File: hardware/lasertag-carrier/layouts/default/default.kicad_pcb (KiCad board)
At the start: 2 copper layers, 100 x 80 mm, 39 parts, among them J0 Power in 2P, J1 S3-Matrix L, J12 Ext button, J13 Touch hdr, J14 Activity LED, J2 S3-Matrix R, J3 MAX98357A, J4 Speaker, J5 microSD, J6 IR RX, J7 IR LED, J8 WS2812 out, J9 OLED I2C, Q1 2N2222A, SW1 SW_PUSH_6mm, SW2 PWR switch

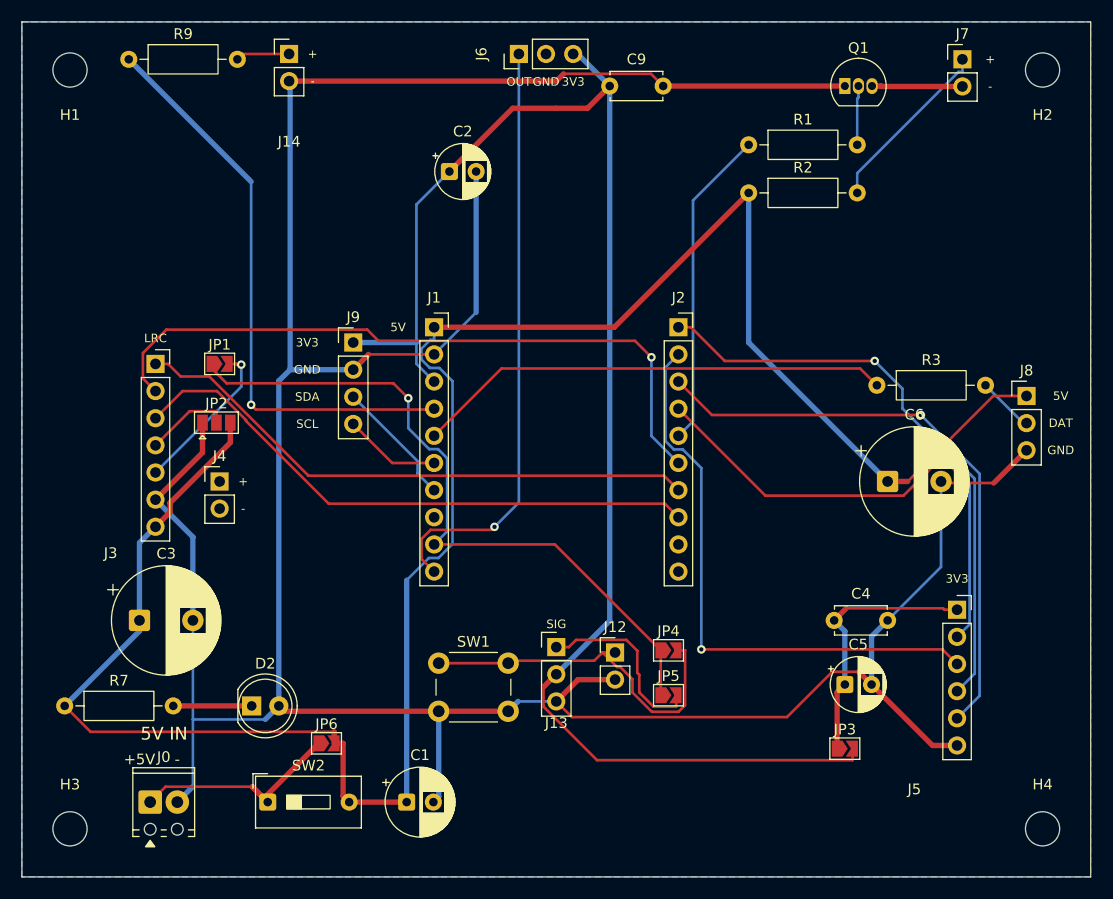
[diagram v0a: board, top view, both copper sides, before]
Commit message: Silk: component values and socket/function names
- resistor values inside each body: 470R/33R (IR), 220R (WS + ACT), 330R (PWR)
- capacitor values alongside: 100u, 10u x2, 470u, 1000u, 100n x2
- 2N2222A by Q1, PWR by D2
- jumper functions: MUTE, GAIN, VDD, BTN, TOUCH, ON
- socket names: AUDIO and microSD rotated under their breakout bodies
  (visible when empty, covered by the module itself once populated),
  plus OLED, WS2812, TOUCH, BTN, SPKR, IR-TX, IR-RX, ACT, PWR
- refdes relocations to clear the new text (J7/J9/JP1/JP6/J12/Q1)

DRC: 0 unconnected, 0 electrical. Three phantom silk_overlap warnings
remain - kicad-cli 10.0.3 pairs reference fields with items 10-60mm away
(J6 ref vs its own segment AND vs WS2812 text 50mm off; C9 ref vs 100n
60mm off). Geometrically impossible; silk Gerber verified.

Fab zip regenerated.

Co-Authored-By: Claude Opus 4.8 <noreply@anthropic.com>
Claude-Session: https://claude.ai/code/session_01TutNLcDSScdeeVSbjpyg8j
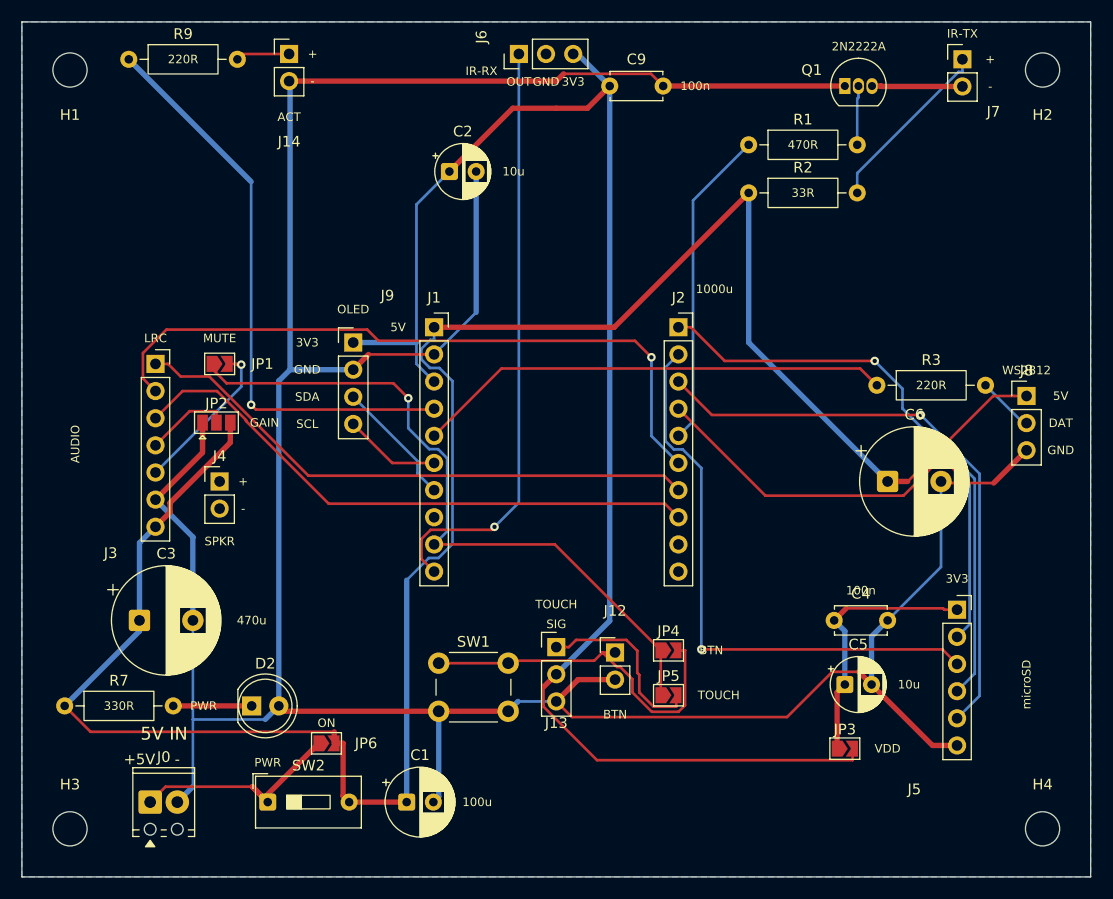
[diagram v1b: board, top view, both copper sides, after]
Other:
- board text added: "1000u"
- board text added: "100n"
- board text added: "100u"
- board text added: "10u"
- board text added: "220R"
- board text added: "2N2222A"
- board text added: "330R"
- board text added: "33R"
- board text added: "470R"
- board text added: "470u"
- board text added: "ACT"
- board text added: "AUDIO"
- board text added: "BTN"
- board text added: "GAIN"
- board text added: "IR-RX"
- board text added: "IR-TX"
- board text added: "MUTE"
- board text added: "OLED"
- board text added: "ON"
- board text added: "PWR"
- board text added: "SPKR"
- board text added: "TOUCH"
- board text added: "VDD"
- board text added: "WS2812"
- board text added: "microSD"

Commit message: Label polish per review; remove superfluous speaker header J4
- 1000u moved inside C6's can (was floating 8mm right of it)
- AUDIO snugged against the J3 socket
- ACT -> ACT LED
- 100n moved inside C9's box (fits between the pads)
- 10u placed vertically beside C5 -- the D5 can physically cannot fit
  0.8mm text between its silk circle and the pad copper (24 arc-segment
  DRC hits proved it)
- J4 removed: its nets appeared nowhere else on the board -- the
  MAX98357A module carries its own speaker terminals (Assumption #10),
  so the header was an unconnected landing pad with no route. BOM and
  i2s_audio.ato updated.

DRC: 0 unconnected, 0 electrical, 3 known-phantom silk warnings.
Fab zip regenerated.

Co-Authored-By: Claude Opus 4.8 <noreply@anthropic.com>
Claude-Session: https://claude.ai/code/session_01TutNLcDSScdeeVSbjpyg8j
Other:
- board text added: "ACT LED"
- board text removed: "ACT"
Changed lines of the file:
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@@
 		)
 	)
-	(gr_text "ACT"
+	(gr_text "ACT LED"
 		(at 125 68.9 0)
 		(layer "F.SilkS")
@@
 		)
 	)
+	(gr_text "1000u"
+		(at 157 82.5 0)
+		(layer "F.SilkS")
+		(effects
+			(font
+				(size 0.8 0.8)
+				(thickness 0.13)
+			)
+		)
+	)
 	(gr_text "100n"
-		(at 163 66 0)
+		(at 157.5 66 0)
 		(layer "F.SilkS")
 		(effects
@@
 		)
 	)
-	(gr_text "1000u"
-		(at 164.8 85 0)
-		(layer "F.SilkS")
-		(effects
-			(font
-				(size 0.8 0.8)
-				(thickness 0.13)
-			)
-		)
-	)
 	(gr_text "TOUCH"
 		(at 165.2 123 0)
@@
 		)
 	)
-	(gr_text "10u"
-		(at 183 122 0)
-		(layer "F.SilkS")
-		(effects
-			(font
-				(size 0.8 0.8)
-				(thickness 0.13)
-			)
-		)
-	)
 	(gr_text "220R"
 		(at 185.08 94 0)
@@
 	)
 	(gr_text "AUDIO"
-		(at 105 99.5 90)
-		(layer "F.SilkS")
-		(effects
+		(at 109.8 99.5 90)
+		(layer "F.SilkS")
+		(effects
+			(font
+				(size 0.8 0.8)
+				(thickness 0.13)
+			)
+		)
+	)
+	(gr_text "10u"
+		(at 182.4 122 90)
+		(layer "F.SilkS")
+		(effects

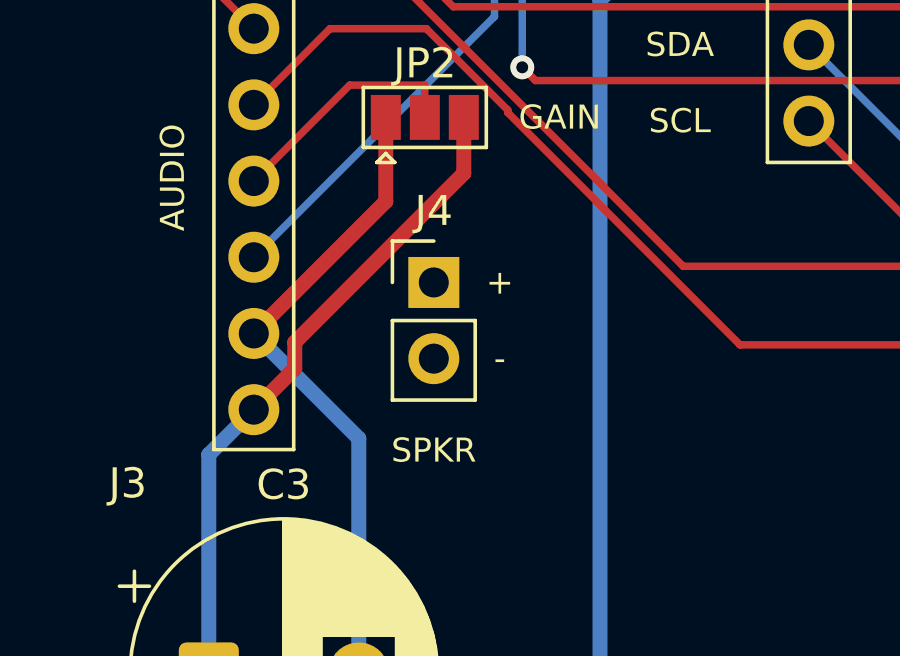
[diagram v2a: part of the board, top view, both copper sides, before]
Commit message: Actually remove J4: pcbnew BOARD.Remove(footprint) silently no-opped
The previous commit claimed J4 was removed but the pcbnew script's
Remove() calls did nothing despite saving without error -- the board
still had 39 footprints and J4 in the BOM. Removed the footprint block
and its three silk texts (SPKR, +, -) textually with verification:
38 footprints, zero J4 references, BOM regenerated without it.

DRC unchanged: 0 unconnected, 0 electrical, 3 known-phantom silk
warnings. Fab zip regenerated from the corrected board.

Co-Authored-By: Claude Opus 4.8 <noreply@anthropic.com>
Claude-Session: https://claude.ai/code/session_01TutNLcDSScdeeVSbjpyg8j
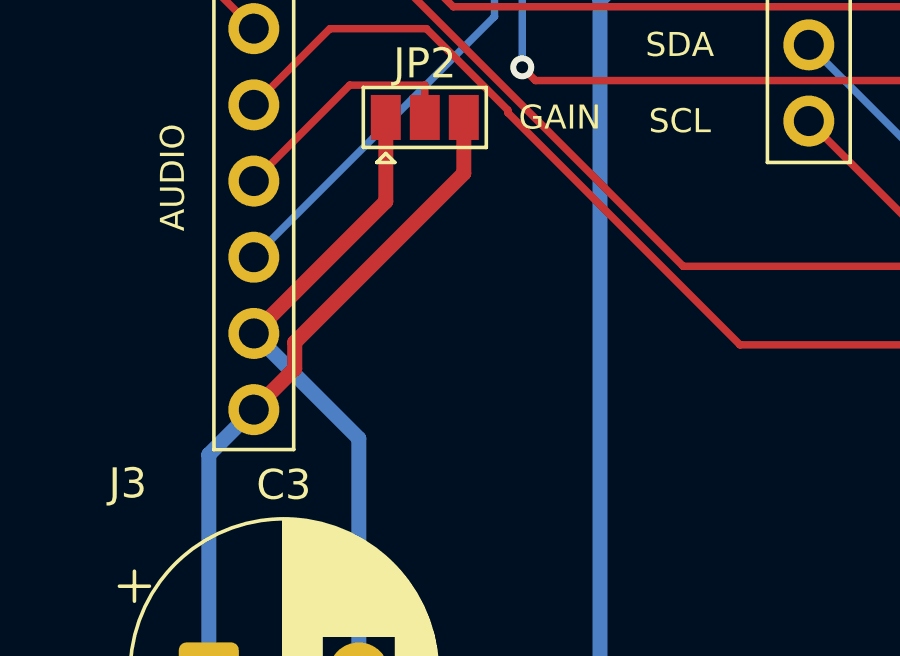
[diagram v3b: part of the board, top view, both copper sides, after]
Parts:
- removed J4: Speaker, Connector_PinHeader_2.54mm:PinHeader_1x02_P2.54mm_Vertical
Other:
- board text removed: "SPKR"
